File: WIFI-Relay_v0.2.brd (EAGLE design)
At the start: 49.2 x 44.4 mm, 38 parts, among them CN1 PBS-3-VERTICAL, CN2 PBS-2-VERTICAL, CN3 PBS-8-1.27-VERTICAL, CN4 PBS-8-1.27-VERTICAL, CN5 PBS-2-VERTICAL, CN6 PBS-2-VERTICAL, CN7 PBS-4-VERTICAL, IC1 74LS595D, IC2 74LS595D, IC3 MC34063AD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

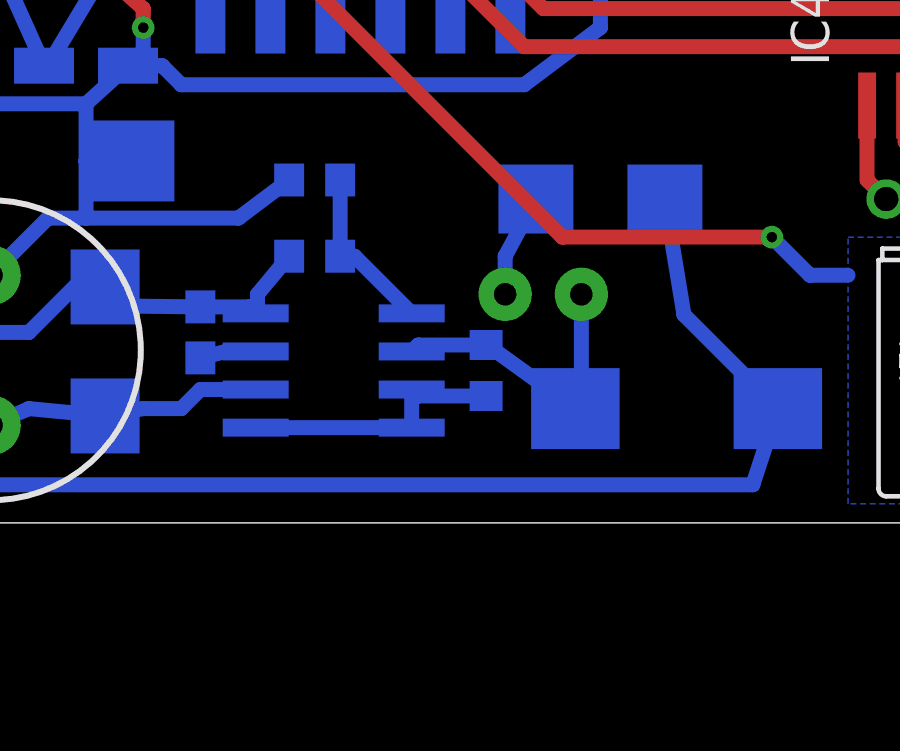
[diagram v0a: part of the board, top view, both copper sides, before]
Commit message: Value and name were changed. Eagle is 9.2.0
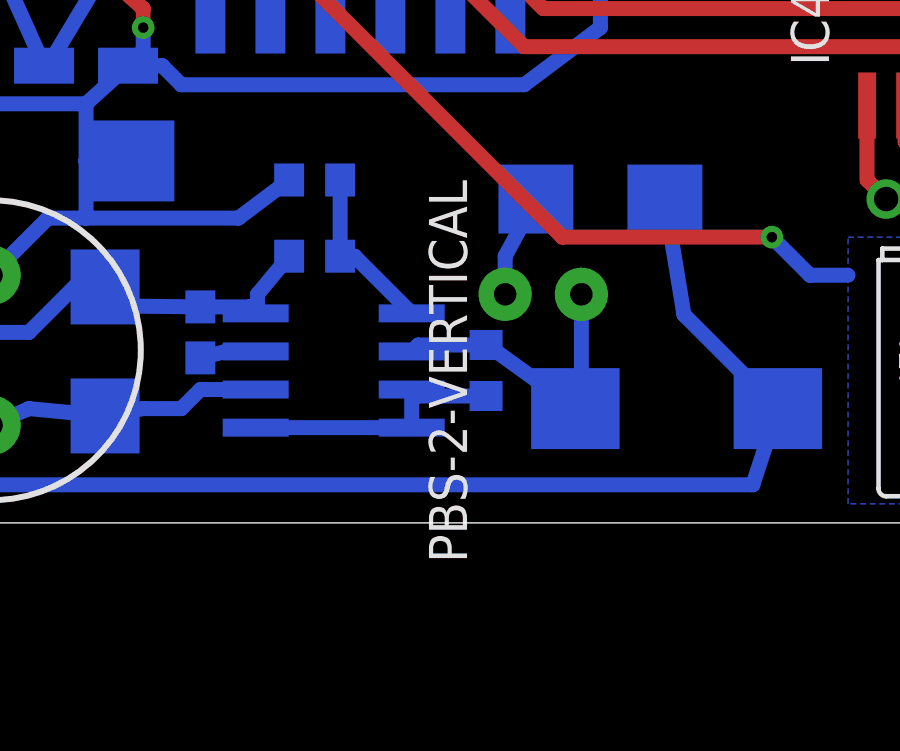
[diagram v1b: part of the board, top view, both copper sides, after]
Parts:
- R10: value 5.1k -> 5.6k
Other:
- board text added: "Polyakov Konstantin Russia, Yeysk 2018-04-26 WFR-0-3-1"
- board text removed: "Polyakov Konstantin Russia, Yeysk, 2018-04-26, v0.3 rev1"
